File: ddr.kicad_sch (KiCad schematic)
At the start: 25 parts, among them U1 MIMX8MM6DVTLZAA, U3 MT40A1G16KD-062E

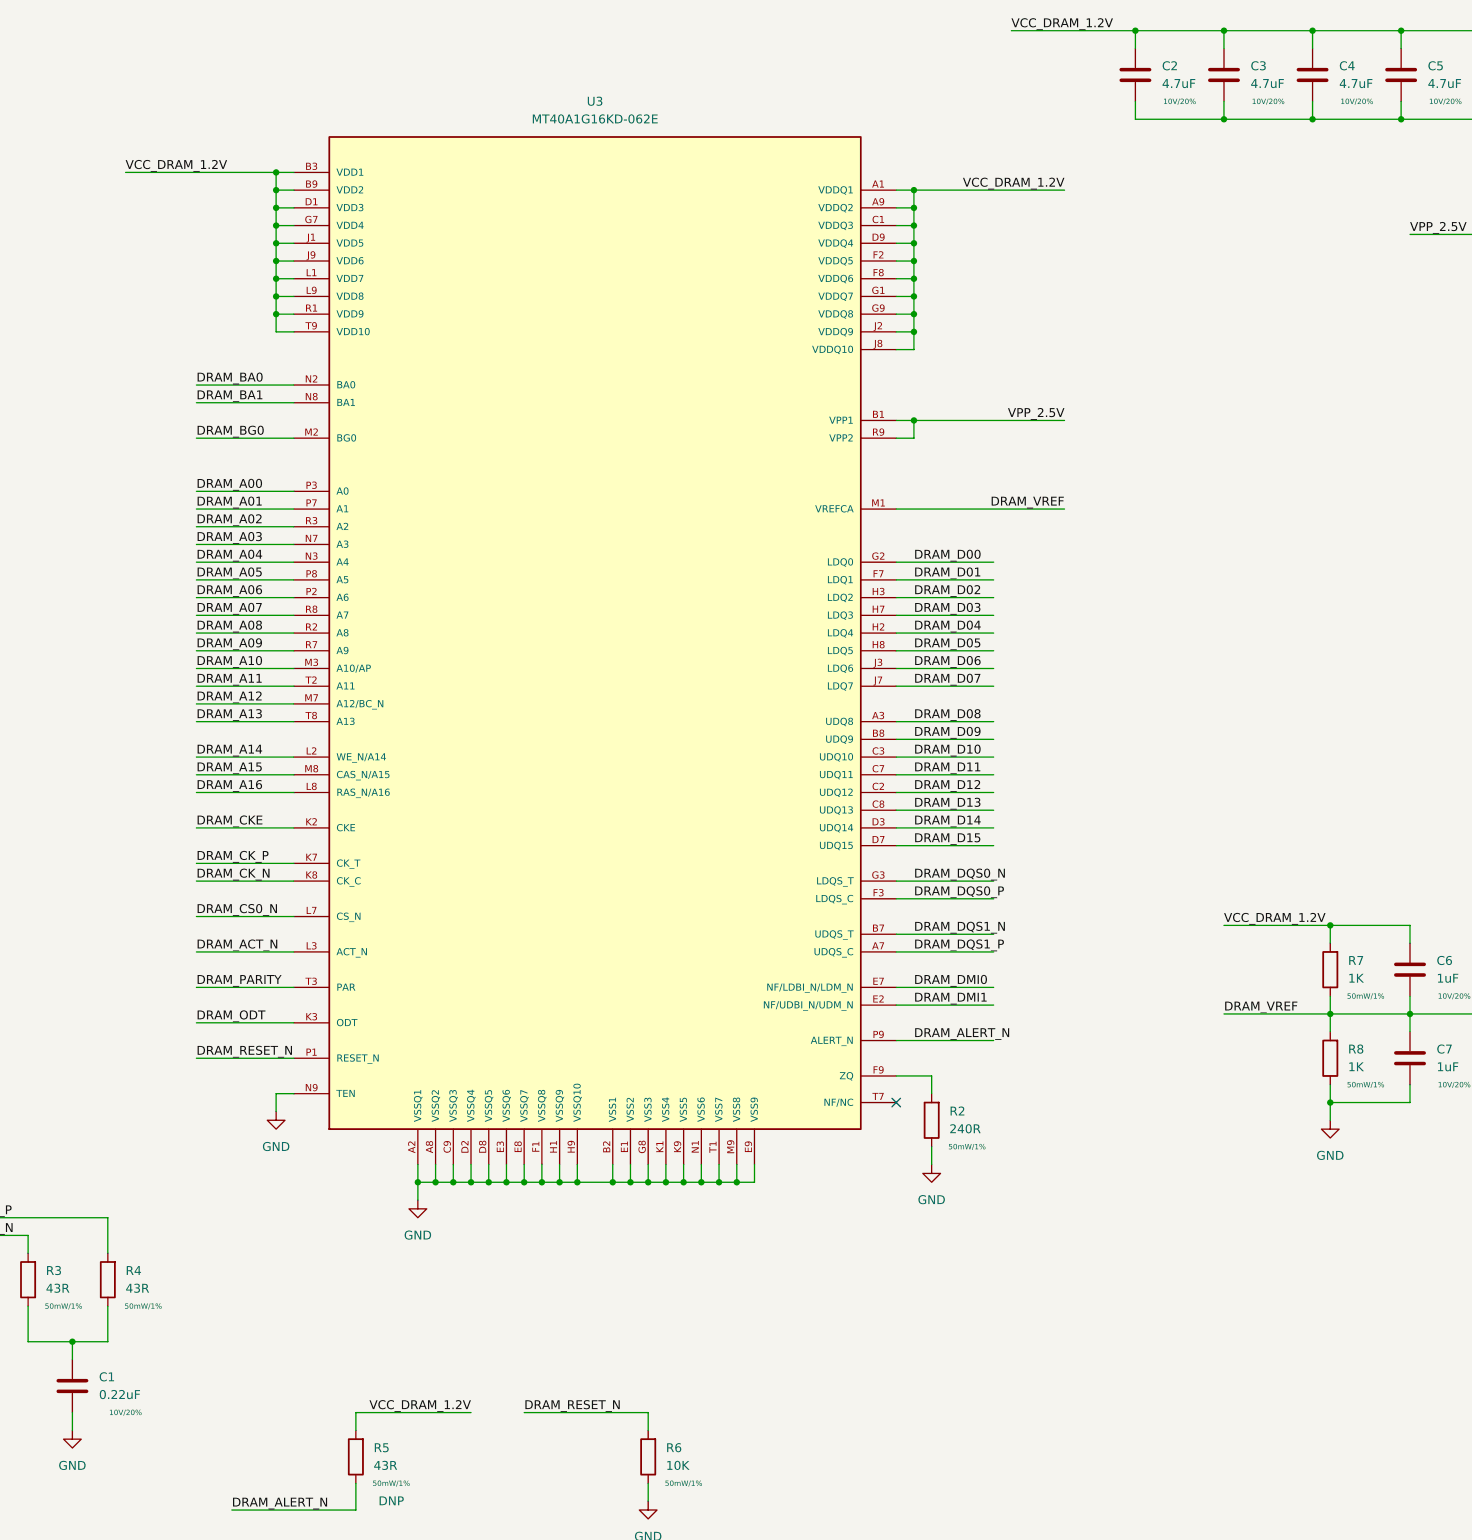
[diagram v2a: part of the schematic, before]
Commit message: storage done, peri work, misc fixes
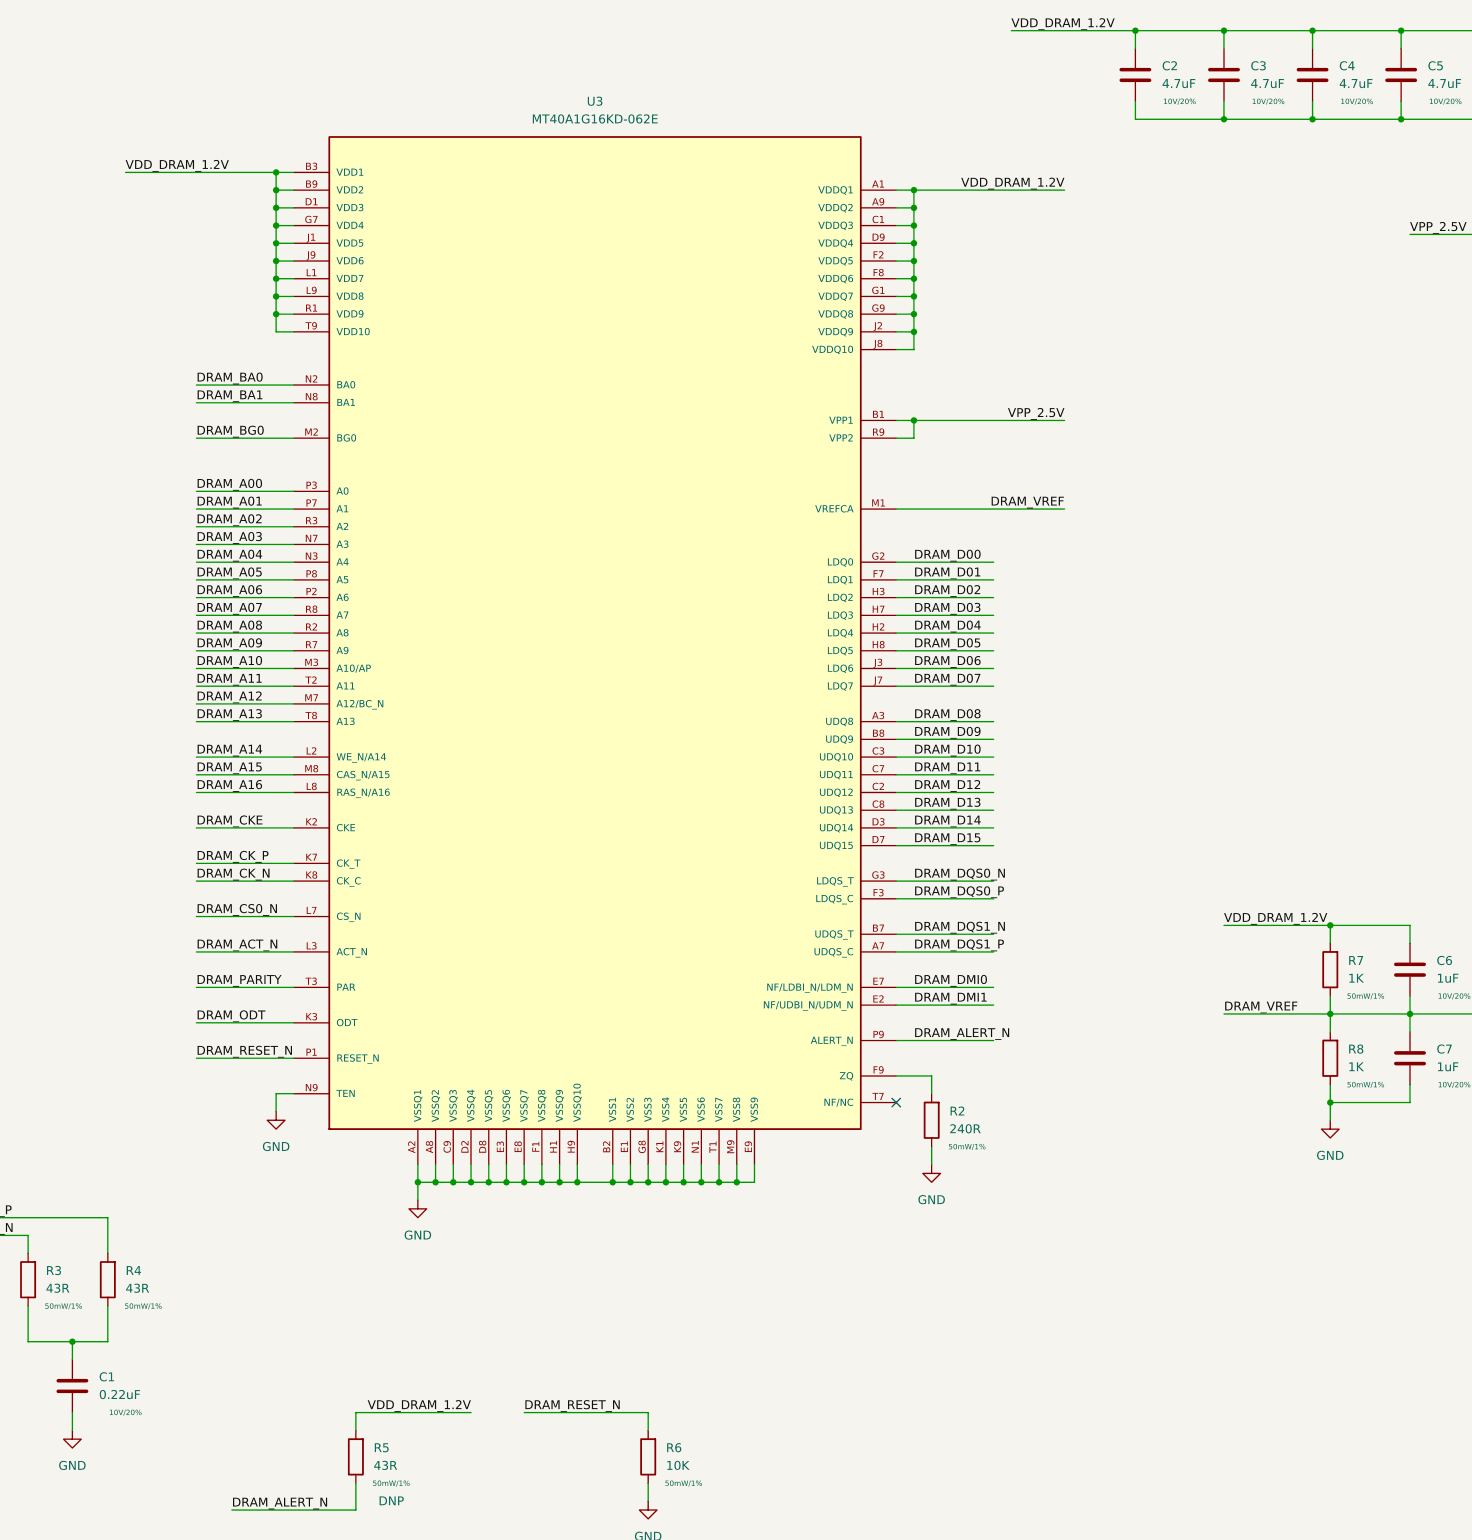
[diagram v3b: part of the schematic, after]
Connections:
- net VCC_DRAM_1.2V renamed VDD_DRAM_1.2V
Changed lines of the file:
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@@
     (effects (font (size 1.27 1.27)) (justify left bottom))
   )
-  (label "VCC_DRAM_1.2V" (at 233.68 231.14 180)
+  (label "VDD_DRAM_1.2V" (at 233.68 231.14 180)
     (effects (font (size 1.27 1.27)) (justify right bottom))
   )
@@
     (effects (font (size 1.27 1.27)) (justify left bottom))
   )
-  (label "VCC_DRAM_1.2V" (at 184.15 53.34 0)
+  (label "VDD_DRAM_1.2V" (at 184.15 53.34 0)
     (effects (font (size 1.27 1.27)) (justify left bottom))
   )
@@
     (effects (font (size 1.27 1.27)) (justify left bottom))
   )
-  (label "VCC_DRAM_1.2V" (at 311.15 33.02 0)
+  (label "VDD_DRAM_1.2V" (at 311.15 33.02 0)
     (effects (font (size 1.27 1.27)) (justify left bottom))
   )
@@
     (effects (font (size 1.27 1.27)) (justify left bottom))
   )
-  (label "VCC_DRAM_1.2V" (at 341.63 161.29 0)
+  (label "VDD_DRAM_1.2V" (at 341.63 161.29 0)
     (effects (font (size 1.27 1.27)) (justify left bottom))
   )
@@
     (effects (font (size 1.27 1.27)) (justify left bottom))
   )
-  (label "VCC_DRAM_1.2V" (at 318.77 55.88 180)
-    (effects (font (size 1.27 1.27)) (justify right bottom))
-  )
+  (label "VDD_DRAM_1.2V" (at 318.77 55.88 180)
+    (effects (font (size 1.27 1.27)) (justify right bottom))
+  )

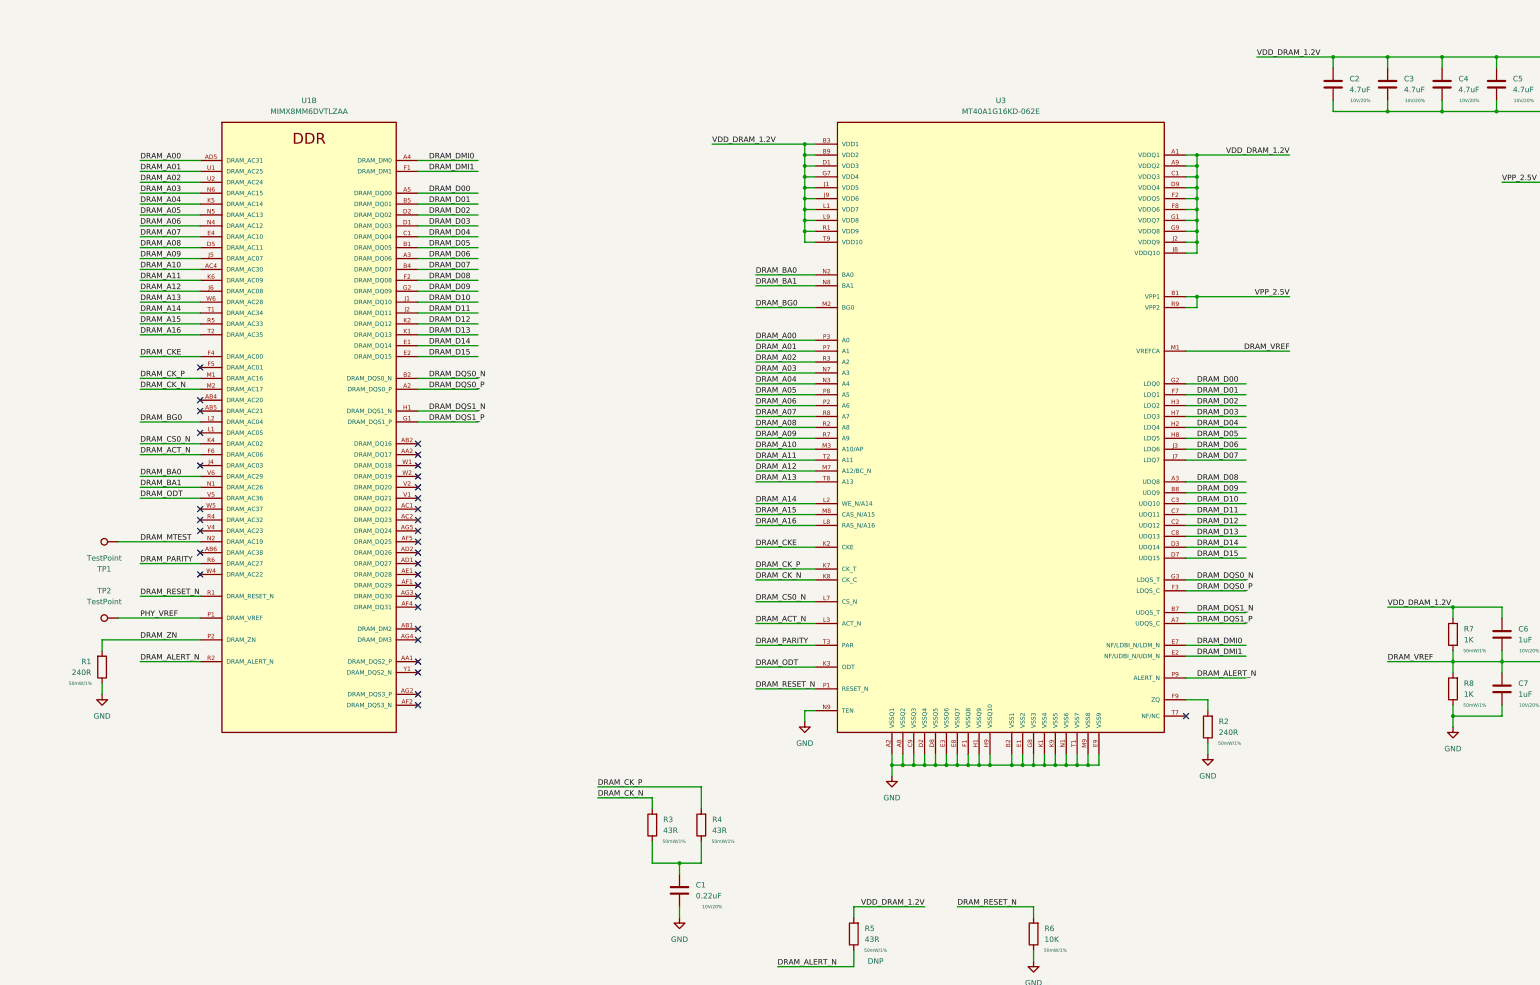
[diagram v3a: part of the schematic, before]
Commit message: ddr: add dual die support, misc work
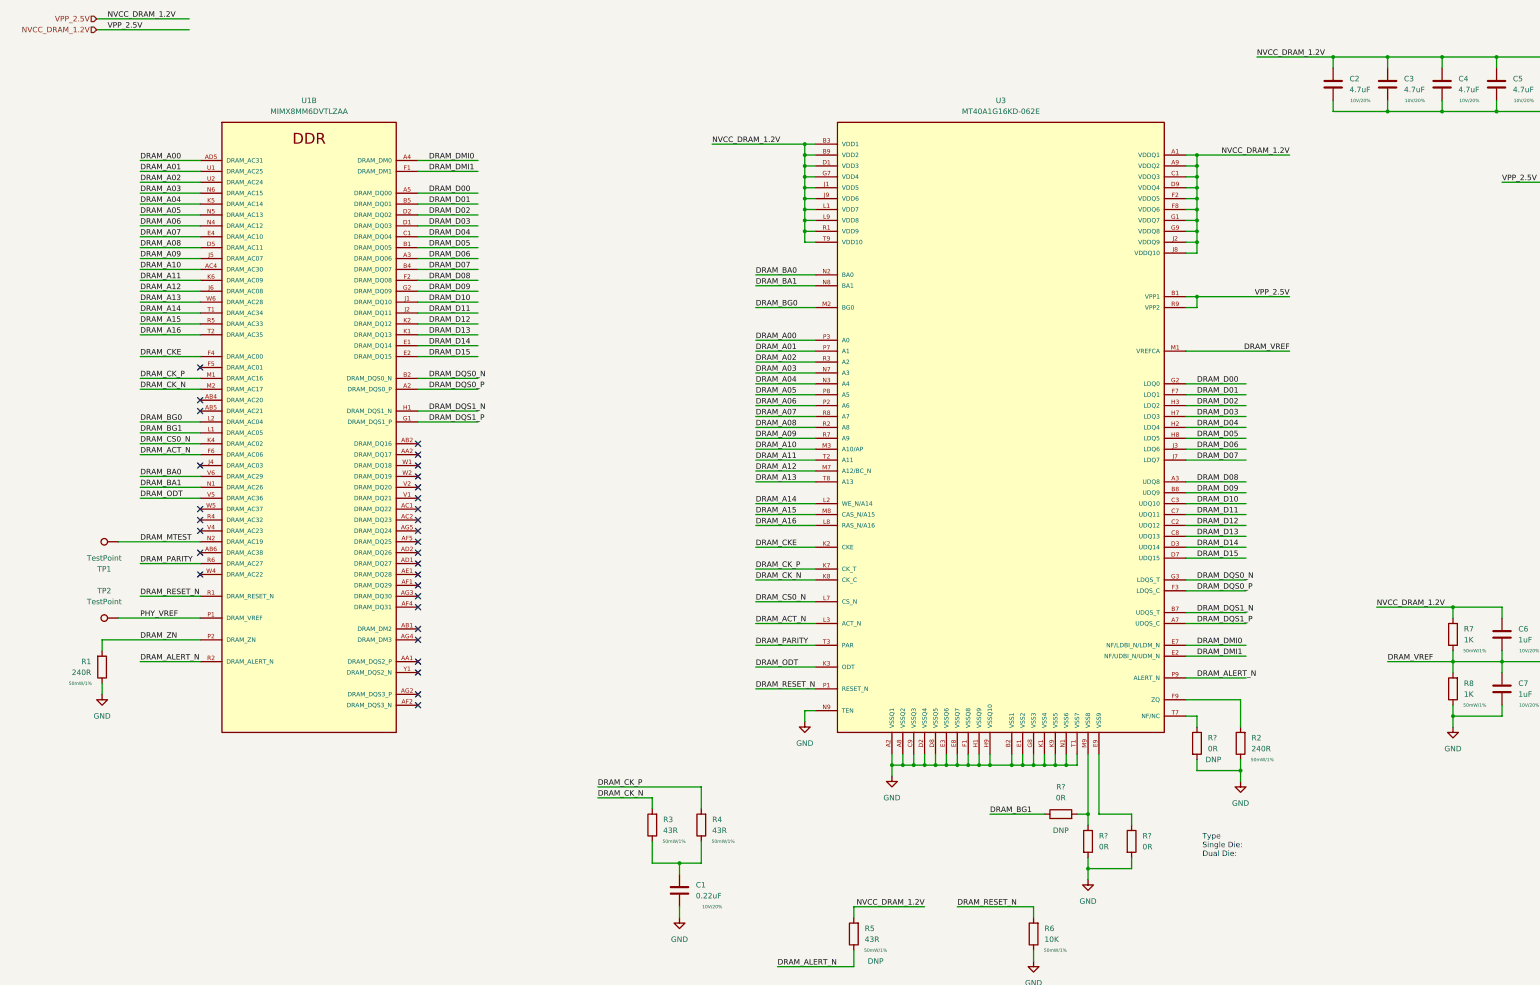
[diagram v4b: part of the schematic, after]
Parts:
- added R? (x4): 0R, Resistor_SMD:R_0402_1005Metric, symbol Device:R
- R1, R2: footprint (none) -> Resistor_SMD:R_0201_0603Metric
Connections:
- net VPP_2.5V is gone; now on net NVCC_DRAM_1.2V: C11.1, C9.1, U3.B1 (VPP1), U3.R9 (VPP2)
- net GND: now also R?.2, R?.2, R?.2; no longer U3.E9 (VSS9), U3.M9 (VSS8)
- net DRAM_BG1: now reaches U1.L1 (DRAM_AC05)
- net DRAM_BG1: now also R?.1
- net at U3.T7 (NF/NC): now also R?.1
- net VDD_DRAM_1.2V renamed NVCC_DRAM_1.2V
- new net: R?.1, R?.2, U3.M9 (VSS8)
- new net: R?.1, U3.E9 (VSS9)
- no-connect marks 33 -> 31
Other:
- note added: "Type Single Die: Dual Die:"
- company: (none) -> Q-LAB
- title: (none) -> QSBC
- moved on the sheet: R2
